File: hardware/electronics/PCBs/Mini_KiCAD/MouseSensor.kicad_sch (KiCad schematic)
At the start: 8 parts, among them U2 ADNS-5050

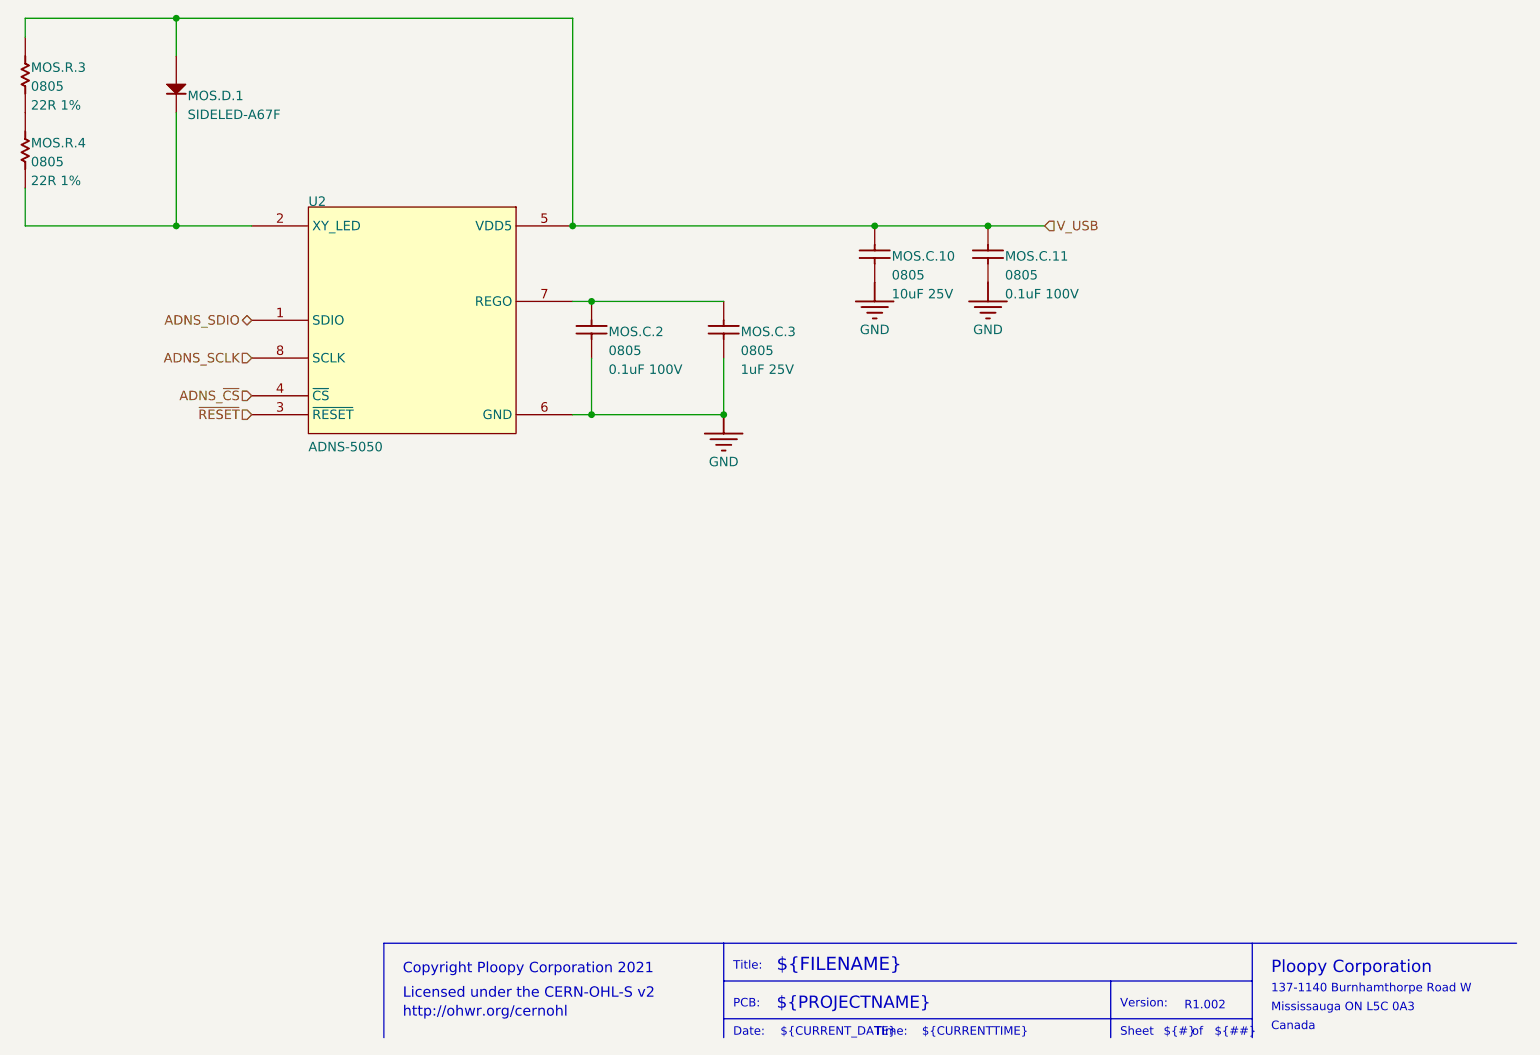
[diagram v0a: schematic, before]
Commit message: Initial commit of the modified Ploopy Mini PCB with RP2040, PMW3360 and mid-mounted USB-C
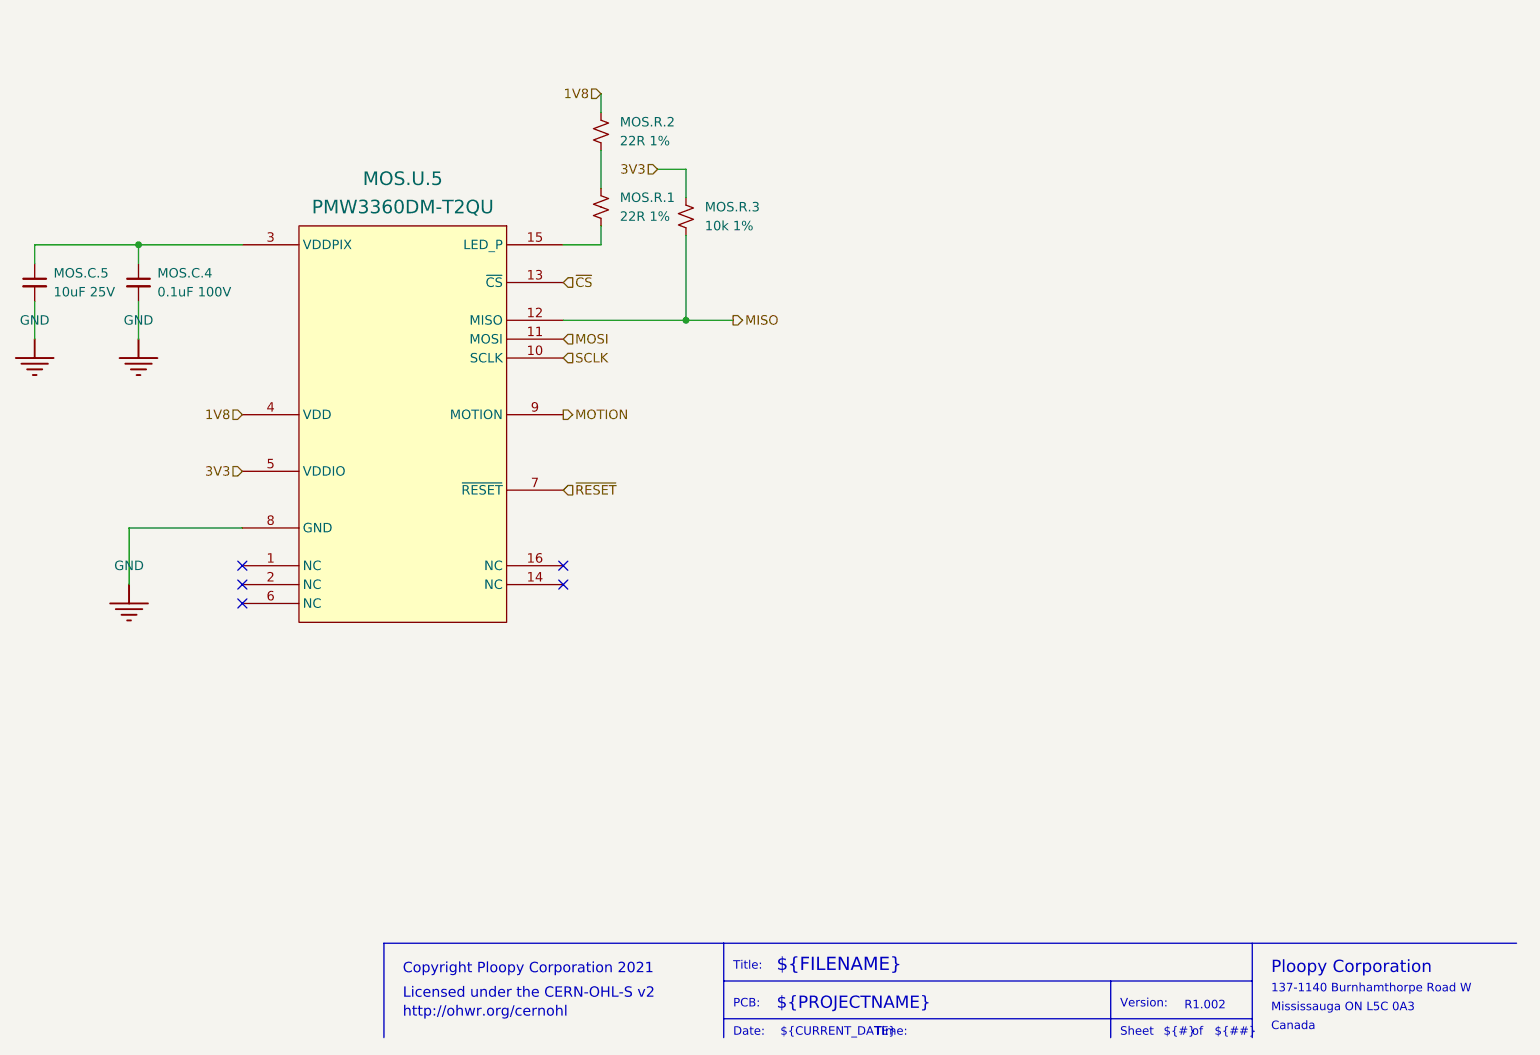
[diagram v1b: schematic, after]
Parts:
- removed MOS.C.10: 0805, 0805 - TALL, symbol Mini-altium-import:MOS_1_Cap 10uF 25V
- removed MOS.C.11, MOS.C.2: 0805, 0805 - TALL, symbol Mini-altium-import:MOS_1_Cap 0.1uF 100V
- removed MOS.C.3: 0805, 0805 - TALL, symbol Mini-altium-import:MOS_1_Cap 1uF 25V
- removed MOS.D.1: SIDELED-A67F, SIDELED-A67F, symbol Mini-altium-import:MOS_1_SIDELED-A67F
- removed MOS.R.3, MOS.R.4: 0805, 0805, symbol Mini-altium-import:MOS_1_Res 22R 1% 0805
- removed U2: ADNS-5050, ADNS-5050, symbol Mini-altium-import:MOS_0_ADNS-5050
- added MOS.C.4: 0.1uF 100V, Chip_Passives.PcbLib:0805, symbol Device:C_Small
- added MOS.C.5: 10uF 25V, Chip_Passives.PcbLib:0805, symbol Device:C_Small
- added MOS.R.1, MOS.R.2: 22R 1%, Chip_Passives.PcbLib:0805, symbol Device:R_Small_US
- added MOS.R.3: 10k 1%, Chip_Passives.PcbLib:0805, symbol Device:R_Small_US
- added MOS.U.5: PMW3360DM-T2QU, OptoElectronics:PMW3360DM-T2QU, symbol OptoElectronics.PcbLib:PMW3360DM-T2QU
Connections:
- net GND: now also MOS.C.4.2, MOS.C.5.2, MOS.U.5.8 (GND)
- net ~{RESET}: now also MOS.U.5.7 (~{RESET})
- new net: MOS.R.1.2, MOS.U.5.15 (LED_P)
- new net: MOS.C.4.1, MOS.C.5.1, MOS.U.5.3 (VDDPIX)
- new net: MOS.R.1.1, MOS.R.2.2
- new net 1V8: MOS.R.2.1, MOS.U.5.4 (VDD)
- new net 3V3: MOS.R.3.1, MOS.U.5.5 (VDDIO)
- new net MISO: MOS.R.3.2, MOS.U.5.12 (MISO)
- new net MOSI: MOS.U.5.11 (MOSI)
- new net MOTION: MOS.U.5.9 (MOTION)
- new net SCLK: MOS.U.5.10 (SCLK)
- new net ~{CS}: MOS.U.5.13 (~{CS})
- no-connect marks 0 -> 5
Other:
- note removed: "${CURRENTTIME}"

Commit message: Rerouted the SPI devices and general cleanup, relocated all associated footprint library inside the project folder
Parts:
- MOS.C.4, MOS.C.5: footprint Chip_Passives.PcbLib:0805 -> Chip_Passives.PcbLib:0805 - TALL
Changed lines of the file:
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@@
 			)
 		)
-		(property "Footprint" "Chip_Passives.PcbLib:0805"
+		(property "Footprint" "Chip_Passives.PcbLib:0805 - TALL"
 			(at 88.9 109.22 0)
 			(effects
@@
 			)
 		)
-		(property "Footprint" "Chip_Passives.PcbLib:0805"
+		(property "Footprint" "Chip_Passives.PcbLib:0805 - TALL"
 			(at 74.93 109.22 0)
 			(effects

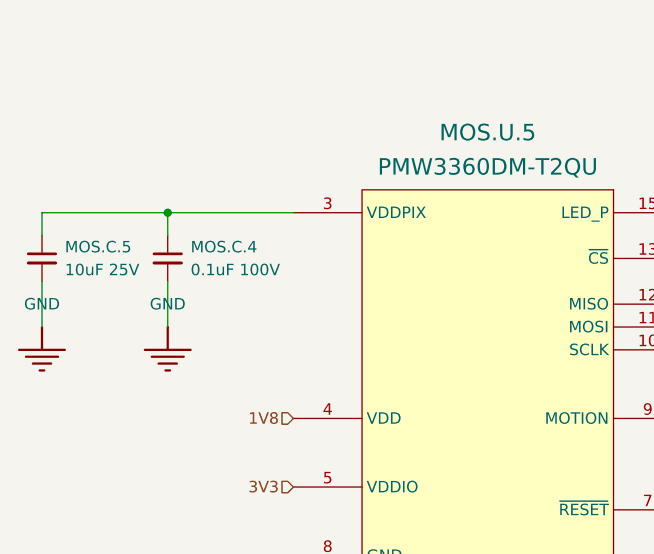
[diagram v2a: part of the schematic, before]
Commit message: Resolved most DRC errors and re-annotated the schematic to be friendly to BOM generation.
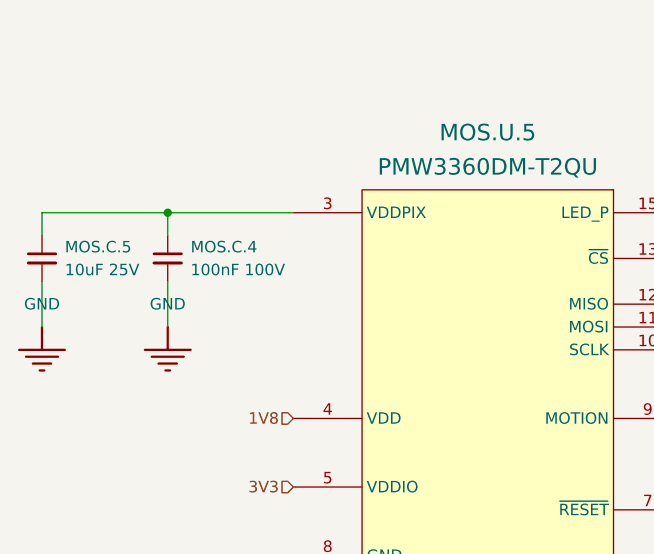
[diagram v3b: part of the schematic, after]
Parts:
- MOS.C.4: value 0.1uF 100V -> 100nF 100V
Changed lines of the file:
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@@
 			)
 		)
-		(property "Value" "0.1uF 100V"
+		(property "Value" "100nF 100V"
 			(at 91.44 110.4962 0)
 			(effects

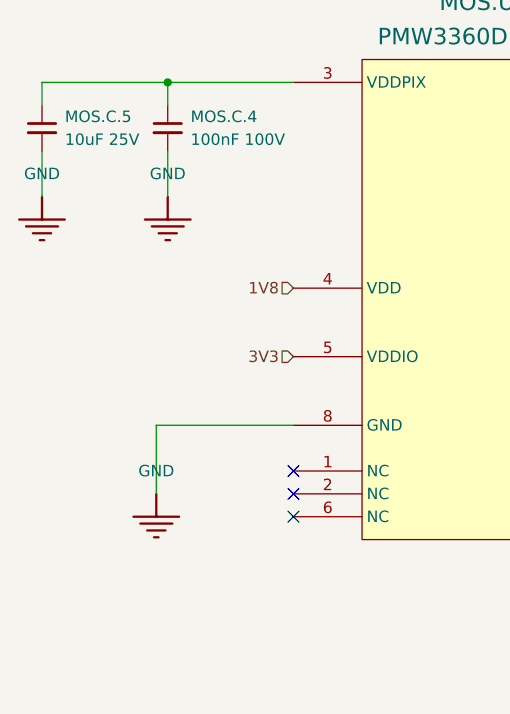
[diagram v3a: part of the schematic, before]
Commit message: Rev1.002 Replaced all symbols in the schematic with built-in symbols where applicable. Reoriented the sensor to solve interference and tracking issues. Replaced the mid-mount USB port with regular port.
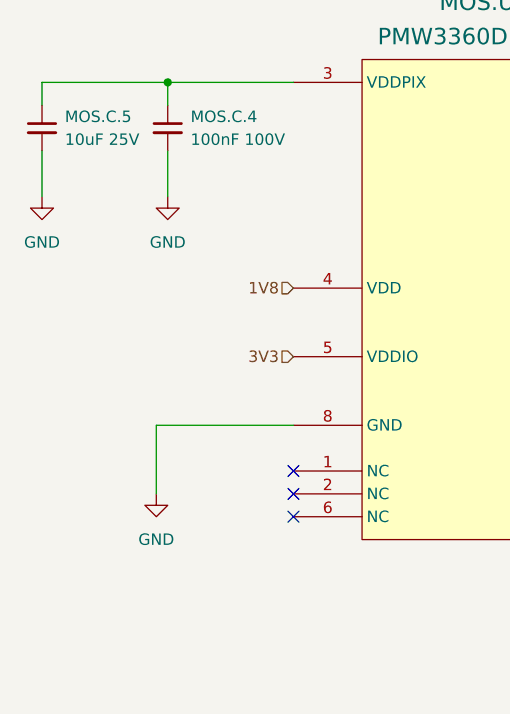
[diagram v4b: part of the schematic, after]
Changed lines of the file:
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@@
 	)
 	(symbol
-		(lib_id "Mini-altium-import:GND_POWER_GROUND")
+		(lib_id "power:GND")
 		(at 88.9 116.84 0)
 		(unit 1)
@@
 		)
 		(property "Value" "GND"
-			(at 88.9 114.3 0)
+			(at 88.9 121.92 0)
 			(effects
 				(font
@@
 			)
 		)
-		(property "Description" "Power symbol creates a global label with name 'GND'"
+		(property "Description" "Power symbol creates a global label with name \"GND\" , ground"
 			(at 88.9 116.84 0)
 			(effects
@@
 			)
 		)
-		(pin ""
+		(pin "1"
 		)
 		(instances
@@
 	)
 	(symbol
-		(lib_id "Mini-altium-import:GND_POWER_GROUND")
+		(lib_id "power:GND")
 		(at 74.93 116.84 0)
 		(unit 1)
@@
 		)
 		(property "Value" "GND"
-			(at 74.93 114.3 0)
+			(at 74.93 121.92 0)
 			(effects
 				(font
@@
 			)
 		)
-		(property "Description" "Power symbol creates a global label with name 'GND'"
+		(property "Description" "Power symbol creates a global label with name \"GND\" , ground"
 			(at 74.93 116.84 0)
 			(effects
@@
 			)
 		)
-		(pin ""
+		(pin "1"
 		)
 		(instances
@@
 	)
 	(symbol
-		(lib_id "Mini-altium-import:GND_POWER_GROUND")
+		(lib_id "power:GND")
 		(at 87.63 149.86 0)
 		(unit 1)
@@
 		)
 		(property "Value" "GND"
-			(at 87.63 147.32 0)
+			(at 87.63 154.94 0)
 			(effects
 				(font
@@
 			)
 		)
-		(property "Description" "Power symbol creates a global label with name 'GND'"
+		(property "Description" "Power symbol creates a global label with name \"GND\" , ground"
 			(at 87.63 149.86 0)
 			(effects
@@
 			)
 		)
-		(pin ""
+		(pin "1"
 		)
 		(instances
